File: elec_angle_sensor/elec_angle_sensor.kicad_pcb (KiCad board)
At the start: 2 copper layers, 20 x 20 mm, 17 parts, among them J1 JST SH, J7 JST SH, U1 AS5600L

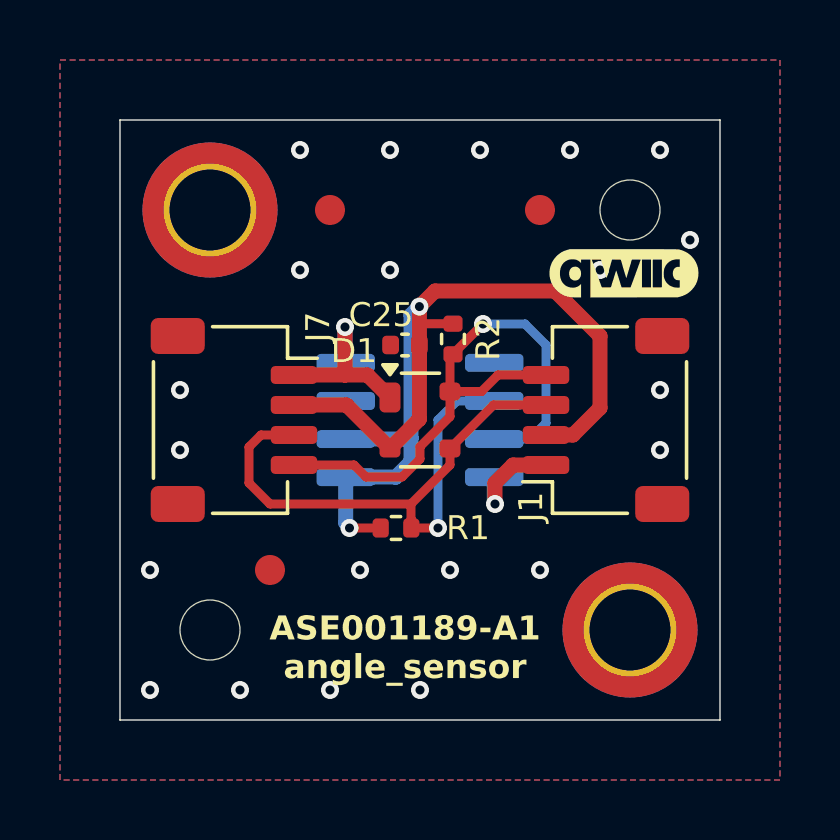
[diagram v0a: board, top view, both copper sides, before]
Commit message: [update] IMU + angle sensor RC1
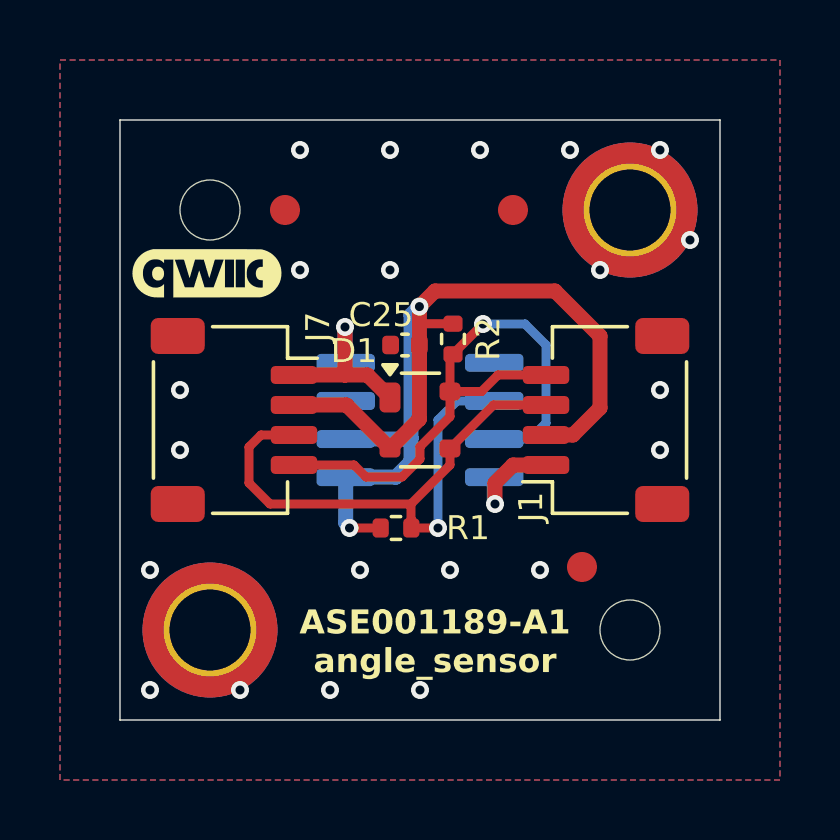
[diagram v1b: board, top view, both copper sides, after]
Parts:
- moved H4 14.0 mm to (137.9, 42.6)
- moved H5 14.0 mm to (123.9, 56.6)
- moved H6 14.0 mm to (137.9, 56.6)
- moved H7 14.0 mm to (123.9, 42.6)
- moved G1 13.9 mm to (123.8, 44.7)
- moved FID3 10.4 mm to (136.3, 54.5)
- moved FID2 1.50 mm to (126.4, 42.6)
- moved H3 1.10 mm to (131.6, 54.4)
- moved FID1 0.90 mm to (134.0, 42.6)
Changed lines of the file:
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@@
 	(footprint "Fiducial:Fiducial_1mm_Mask2mm"
 		(layer "F.Cu")
-		(at 125.897501 54.640001)
+		(at 136.297501 54.540001)
 		(descr "Fiducial, circular marking, 1mm bare copper, 2mm soldermask opening (Level A)")
 		(tags "fiducial")
@@
 	)
 	(footprint "MountingHole:MountingHole_2.7mm_M2.5_ISO7380_Pad_TopBottom"
-		(locked yes)
 		(layer "F.Cu")
-		(at 123.897501 42.640001)
+		(at 137.897501 42.640001)
 		(descr "Mounting Hole 2.7mm, M2.5, generated by kicad-footprint-generator mountinghole.py")
 		(tags "mountinghole M2.5 ISO7380")
@@
 	)
 	(footprint "Library_Pollen:MountingHole_2.0mm"
-		(locked yes)
 		(layer "F.Cu")
-		(at 123.897501 56.640001)
+		(at 137.897501 56.640001)
 		(descr "Mounting Hole 2.1mm, no annular")
 		(tags "mounting hole 2.1mm no annular")
@@
 	(footprint "Fiducial:Fiducial_1mm_Mask2mm"
 		(layer "F.Cu")
-		(at 127.897501 42.640001)
+		(at 126.397501 42.640001)
 		(descr "Fiducial, circular marking, 1mm bare copper, 2mm soldermask opening (Level A)")
 		(tags "fiducial")
@@
 	)
 	(footprint "MountingHole:MountingHole_2.7mm_M2.5_ISO7380_Pad_TopBottom"
-		(locked yes)
 		(layer "F.Cu")
-		(at 137.897501 56.640001)
+		(at 123.897501 56.640001)
 		(descr "Mounting Hole 2.7mm, M2.5, generated by kicad-footprint-generator mountinghole.py")
 		(tags "mountinghole M2.5 ISO7380")
@@
 	)
 	(footprint "Library_Pollen:MountingHole_2.0mm"
-		(locked yes)
 		(layer "F.Cu")
-		(at 137.897501 42.640001)
+		(at 123.897501 42.640001)
 		(descr "Mounting Hole 2.1mm, no annular")
 		(tags "mounting hole 2.1mm no annular")
@@
 	(footprint "Fiducial:Fiducial_1mm_Mask2mm"
 		(layer "F.Cu")
-		(at 134.897501 42.640001)
+		(at 133.997501 42.640001)
 		(descr "Fiducial, circular marking, 1mm bare copper, 2mm soldermask opening (Level A)")
 		(tags "fiducial")
@@
 	(footprint "Library_Pollen:Logo_qwiic_5mm"
 		(layer "F.Cu")
-		(at 137.697501 44.740001)
+		(at 123.797501 44.740001)
 		(tags "SparkFun")
 		(property "Reference" "G1"
@@
 	(footprint "Library_Pollen:Logo_Pollen_2021_sq"
 		(layer "B.Cu")
-		(at 130.500104 54.445192 180)
+		(at 131.600104 54.445192 180)
 		(property "Reference" "H3"
 			(at 0 0.5 0)
@@
 	)
 	(gr_rect
+		(start 123.897501 42.640001)
+		(end 137.897501 56.640001)
+		(stroke
+			(width 0.1)
+			(type default)
+		)
+		(fill no)
+		(layer "Dwgs.User")
+	)
+	(gr_rect
 		(start 120.897501 39.640001)
 		(end 140.897501 59.640001)
@@
 	)
 	(gr_text "ASE001189-A1\nangle_sensor"
-		(at 130.397501 58.340001 0)
+		(at 131.397501 58.140001 0)
 		(layer "F.SilkS" knockout)
 		(effects
